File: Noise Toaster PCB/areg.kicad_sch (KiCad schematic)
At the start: 18 parts, among them Q1 2N3906, Q9 2N5457, U2 LM324

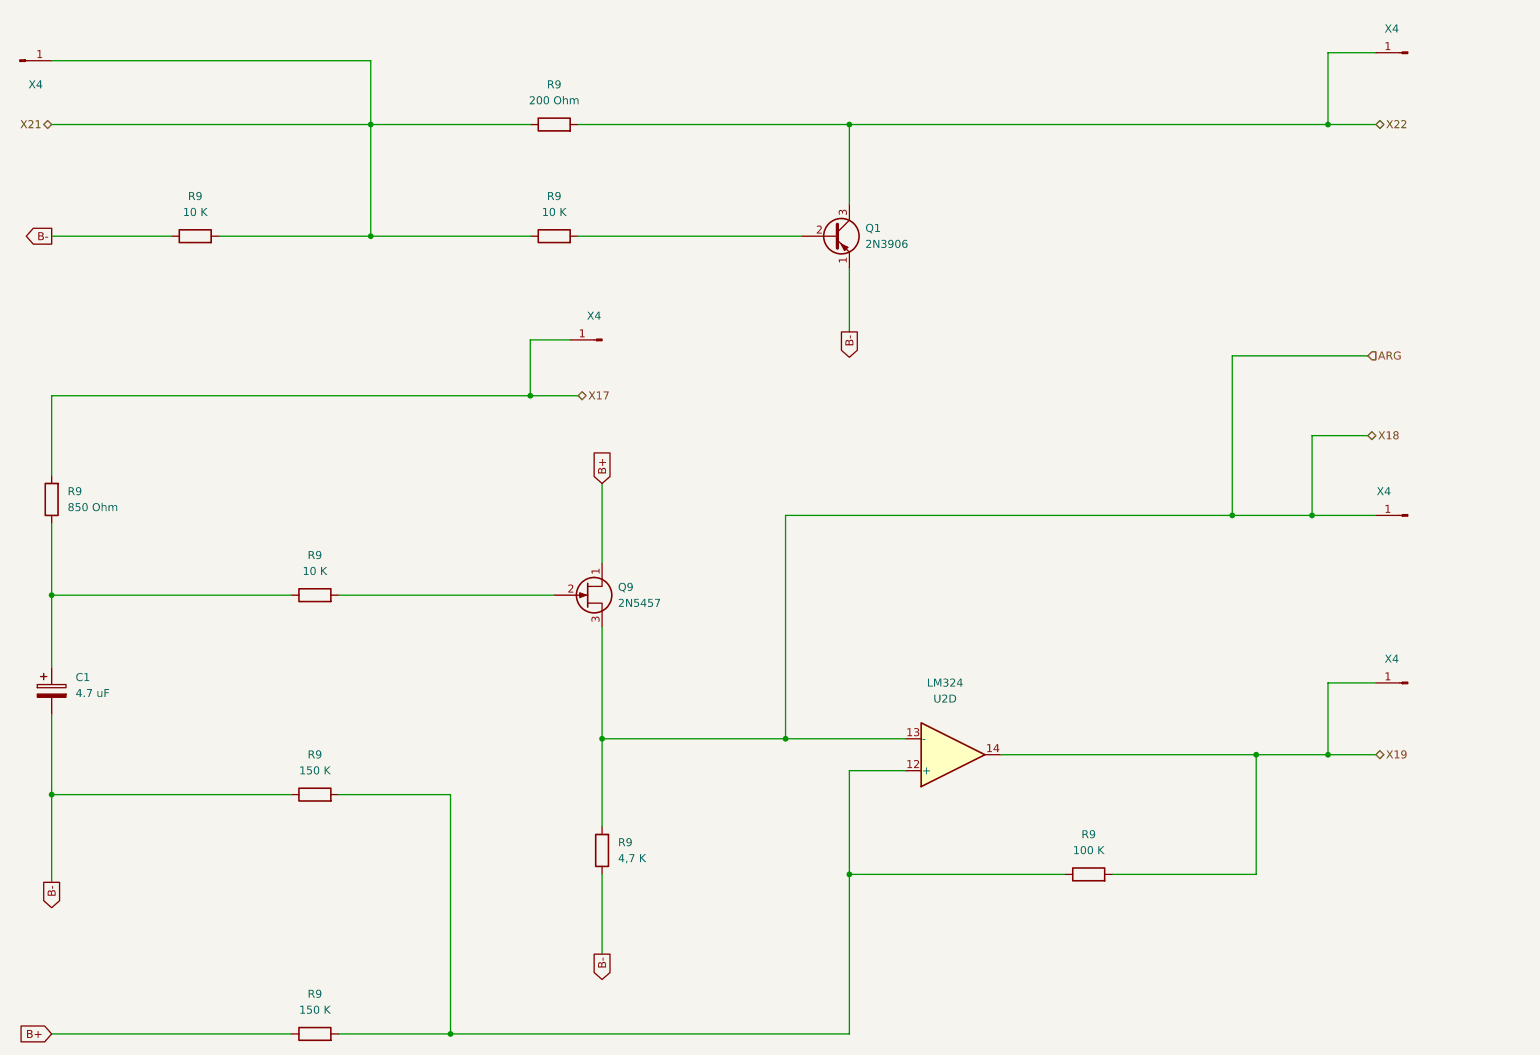
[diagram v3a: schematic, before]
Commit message: wireing and components have been checked
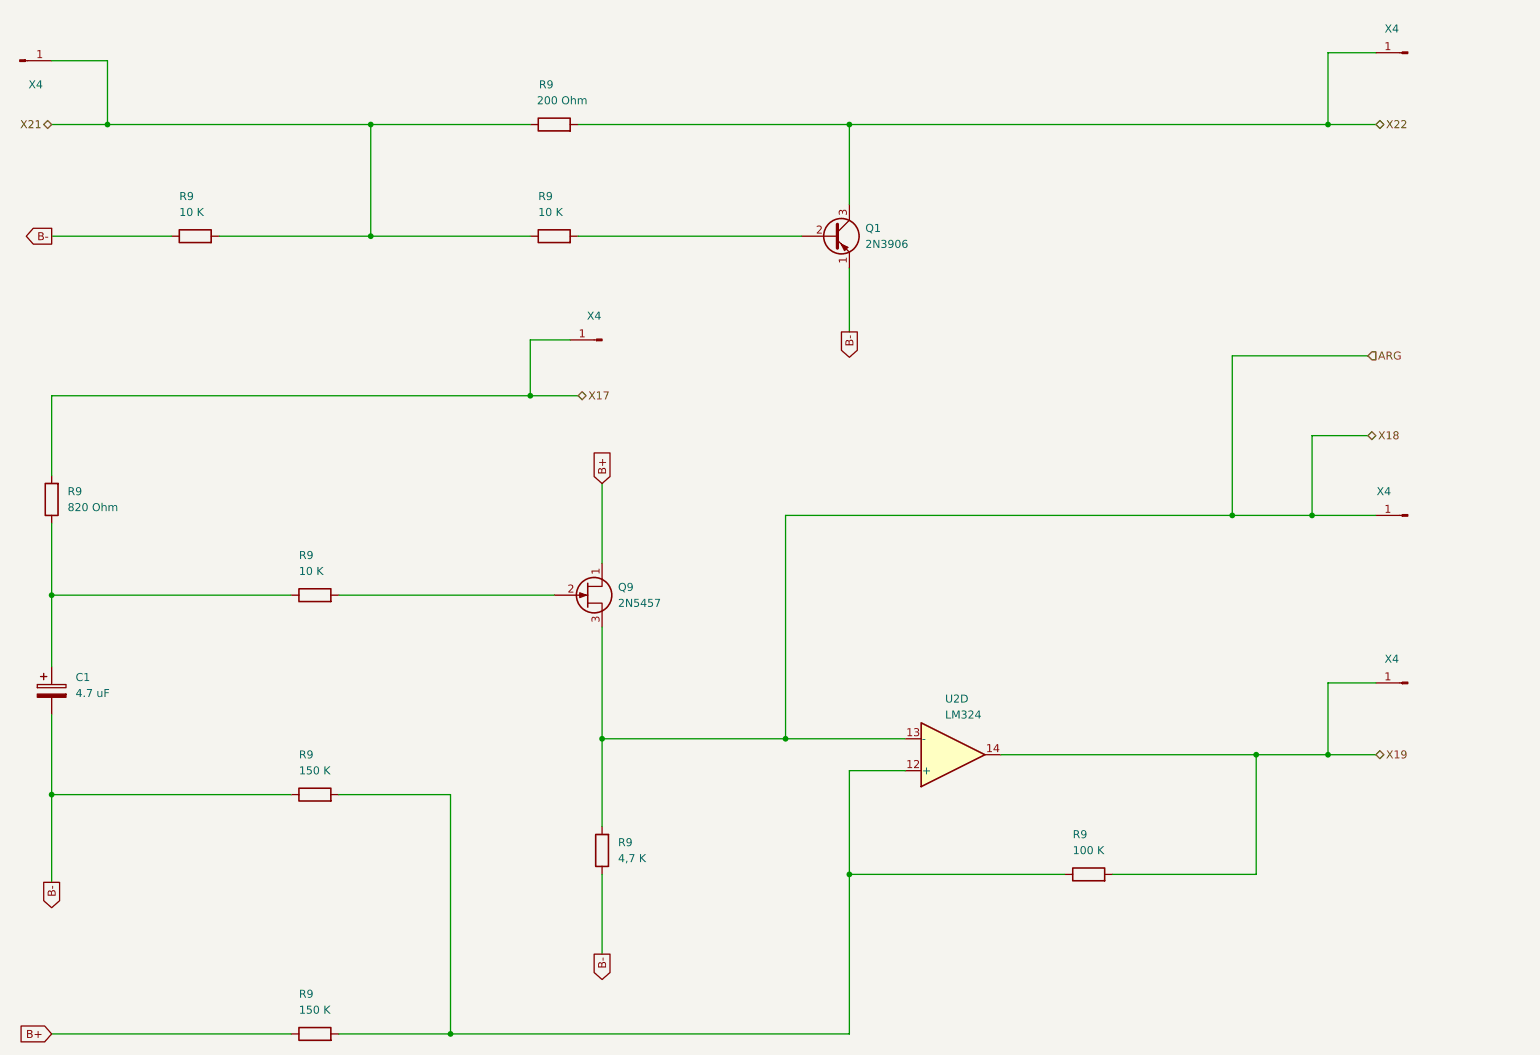
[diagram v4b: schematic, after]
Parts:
- R9: value 850 Ohm -> 820 Ohm
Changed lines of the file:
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@@
   (junction (at 241.3 33.02) (diameter 0) (color 0 0 0 0)
   )
+  (junction (at 46.99 33.02) (diameter 0) (color 0 0 0 0)
+  )
   (junction (at 114.3 76.2) (diameter 0) (color 0 0 0 0)
   )
@@
     (stroke (width 0) (type default))
   )
-  (wire (pts (xy 88.9 22.86) (xy 88.9 33.02))
+  (wire (pts (xy 46.99 22.86) (xy 46.99 33.02))
     (stroke (width 0) (type default))
   )
@@
     (stroke (width 0) (type default))
   )
-  (wire (pts (xy 38.1 33.02) (xy 88.9 33.02))
+  (wire (pts (xy 38.1 33.02) (xy 46.99 33.02))
     (stroke (width 0) (type default))
   )
@@
     (stroke (width 0) (type default))
   )
-  (wire (pts (xy 38.1 22.86) (xy 88.9 22.86))
+  (wire (pts (xy 38.1 22.86) (xy 46.99 22.86))
     (stroke (width 0) (type default))
   )
@@
   )
   (wire (pts (xy 114.3 76.2) (xy 121.92 76.2))
+    (stroke (width 0) (type default))
+  )
+  (wire (pts (xy 46.99 33.02) (xy 88.9 33.02))
     (stroke (width 0) (type default))
   )
@@
     (in_bom yes) (on_board yes) (dnp no)
     (property "Reference" "U2" (at 180.34 124.46 0)
-      (effects (font (size 1.27 1.27)))
-    )
-    (property "Value" "LM324" (at 180.34 121.92 0)
-      (effects (font (size 1.27 1.27)))
+      (effects (font (size 1.27 1.27)) (justify left))
+    )
+    (property "Value" "LM324" (at 180.34 127 0)
+      (effects (font (size 1.27 1.27)) (justify left))
     )
     (property "Footprint" "" (at 180.34 135.89 0)
@@
   )
   (symbol (lib_id "Device:R") (at 60.96 50.8 90) (unit 1)
-    (in_bom yes) (on_board yes) (dnp no) (fields_autoplaced)
-    (property "Reference" "R9" (at 60.96 44.45 90)
-      (effects (font (size 1.27 1.27)))
-    )
-    (property "Value" "10 K" (at 60.96 46.99 90)
-      (effects (font (size 1.27 1.27)))
+    (in_bom yes) (on_board yes) (dnp no)
+    (property "Reference" "R9" (at 58.42 44.45 90)
+      (effects (font (size 1.27 1.27)) (justify right))
+    )
+    (property "Value" "10 K" (at 58.42 46.99 90)
+      (effects (font (size 1.27 1.27)) (justify right))
     )
     (property "Footprint" "" (at 60.96 52.578 90)
@@
       (effects (font (size 1.27 1.27)) (justify right))
     )
-    (property "Value" "850 Ohm" (at 40.64 93.98 0)
+    (property "Value" "820 Ohm" (at 40.64 93.98 0)
       (effects (font (size 1.27 1.27)) (justify right))
     )
@@
   (symbol (lib_id "Device:R") (at 80.01 139.7 90) (unit 1)
     (in_bom yes) (on_board yes) (dnp no)
-    (property "Reference" "R9" (at 80.01 133.35 90)
-      (effects (font (size 1.27 1.27)))
-    )
-    (property "Value" "150 K" (at 80.01 135.89 90)
-      (effects (font (size 1.27 1.27)))
+    (property "Reference" "R9" (at 77.47 133.35 90)
+      (effects (font (size 1.27 1.27)) (justify right))
+    )
+    (property "Value" "150 K" (at 77.47 135.89 90)
+      (effects (font (size 1.27 1.27)) (justify right))
     )
     (property "Footprint" "" (at 80.01 141.478 90)
@@
   )
   (symbol (lib_id "Device:R") (at 80.01 107.95 90) (unit 1)
-    (in_bom yes) (on_board yes) (dnp no) (fields_autoplaced)
-    (property "Reference" "R9" (at 80.01 101.6 90)
-      (effects (font (size 1.27 1.27)))
-    )
-    (property "Value" "10 K" (at 80.01 104.14 90)
-      (effects (font (size 1.27 1.27)))
+    (in_bom yes) (on_board yes) (dnp no)
+    (property "Reference" "R9" (at 77.47 101.6 90)
+      (effects (font (size 1.27 1.27)) (justify right))
+    )
+    (property "Value" "10 K" (at 77.47 104.14 90)
+      (effects (font (size 1.27 1.27)) (justify right))
     )
     (property "Footprint" "" (at 80.01 109.728 90)
@@
   )
   (symbol (lib_id "Device:R") (at 118.11 50.8 90) (unit 1)
-    (in_bom yes) (on_board yes) (dnp no) (fields_autoplaced)
-    (property "Reference" "R9" (at 118.11 44.45 90)
-      (effects (font (size 1.27 1.27)))
-    )
-    (property "Value" "10 K" (at 118.11 46.99 90)
-      (effects (font (size 1.27 1.27)))
+    (in_bom yes) (on_board yes) (dnp no)
+    (property "Reference" "R9" (at 115.57 44.45 90)
+      (effects (font (size 1.27 1.27)) (justify right))
+    )
+    (property "Value" "10 K" (at 115.57 46.99 90)
+      (effects (font (size 1.27 1.27)) (justify right))
     )
     (property "Footprint" "" (at 118.11 52.578 90)
@@
   )
   (symbol (lib_id "Device:R") (at 203.2 152.4 90) (unit 1)
-    (in_bom yes) (on_board yes) (dnp no) (fields_autoplaced)
-    (property "Reference" "R9" (at 203.2 146.05 90)
-      (effects (font (size 1.27 1.27)))
-    )
-    (property "Value" "100 K" (at 203.2 148.59 90)
-      (effects (font (size 1.27 1.27)))
+    (in_bom yes) (on_board yes) (dnp no)
+    (property "Reference" "R9" (at 200.66 146.05 90)
+      (effects (font (size 1.27 1.27)) (justify right))
+    )
+    (property "Value" "100 K" (at 200.66 148.59 90)
+      (effects (font (size 1.27 1.27)) (justify right))
     )
     (property "Footprint" "" (at 203.2 154.178 90)
@@
   )
   (symbol (lib_id "Device:R") (at 118.11 33.02 90) (unit 1)
-    (in_bom yes) (on_board yes) (dnp no) (fields_autoplaced)
-    (property "Reference" "R9" (at 118.11 26.67 90)
-      (effects (font (size 1.27 1.27)))
-    )
-    (property "Value" "200 Ohm" (at 118.11 29.21 90)
+    (in_bom yes) (on_board yes) (dnp no)
+    (property "Reference" "R9" (at 116.84 26.67 90)
+      (effects (font (size 1.27 1.27)))
+    )
+    (property "Value" "200 Ohm" (at 119.38 29.21 90)
       (effects (font (size 1.27 1.27)))
     )
@@
   )
   (symbol (lib_id "Device:R") (at 80.01 177.8 90) (unit 1)
-    (in_bom yes) (on_board yes) (dnp no) (fields_autoplaced)
-    (property "Reference" "R9" (at 80.01 171.45 90)
-      (effects (font (size 1.27 1.27)))
-    )
-    (property "Value" "150 K" (at 80.01 173.99 90)
-      (effects (font (size 1.27 1.27)))
+    (in_bom yes) (on_board yes) (dnp no)
+    (property "Reference" "R9" (at 77.47 171.45 90)
+      (effects (font (size 1.27 1.27)) (justify right))
+    )
+    (property "Value" "150 K" (at 77.47 173.99 90)
+      (effects (font (size 1.27 1.27)) (justify right))
     )
     (property "Footprint" "" (at 80.01 179.578 90)

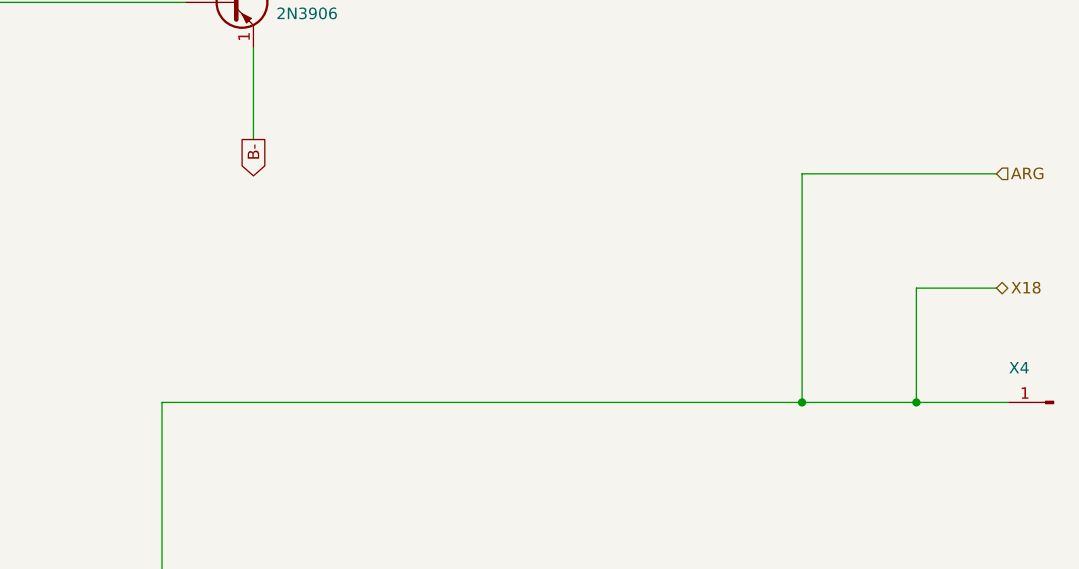
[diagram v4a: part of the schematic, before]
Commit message: applied footprints
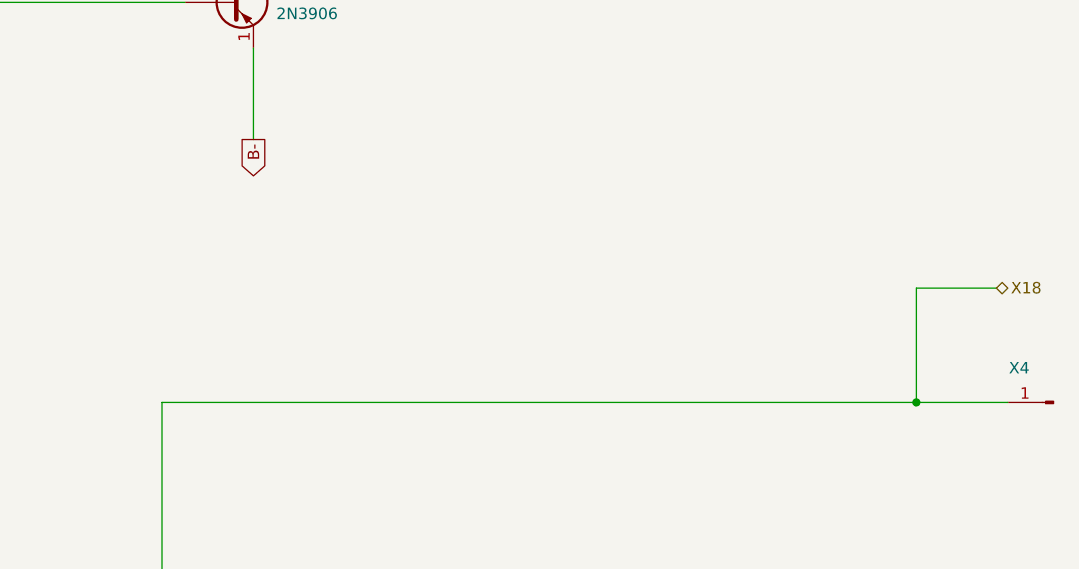
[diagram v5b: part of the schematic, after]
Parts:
- C1: footprint (none) -> Capacitor_THT:CP_Radial_D4.0mm_P1.50mm
- Q9: footprint (none) -> Package_TO_SOT_THT:TO-92_Inline
- R9: footprint (none) -> Resistor_THT:R_Axial_DIN0207_L6.3mm_D2.5mm_P10.16mm_Horizontal
- U2: footprint (none) -> Package_DIP:DIP-14_W7.62mm_Socket
- X4: footprint (none) -> Connector_PinHeader_1.00mm:PinHeader_1x01_P1.00mm_Vertical
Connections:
- net ARG renamed X18
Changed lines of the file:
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@@
   (junction (at 238.76 95.25) (diameter 0) (color 0 0 0 0)
   )
-  (junction (at 226.06 95.25) (diameter 0) (color 0 0 0 0)
-  )
   (junction (at 241.3 133.35) (diameter 0) (color 0 0 0 0)
   )
@@
     (stroke (width 0) (type default))
   )
-  (wire (pts (xy 226.06 69.85) (xy 226.06 95.25))
-    (stroke (width 0) (type default))
-  )
   (wire (pts (xy 248.92 95.25) (xy 238.76 95.25))
     (stroke (width 0) (type default))
@@
     (stroke (width 0) (type default))
   )
-  (wire (pts (xy 226.06 95.25) (xy 238.76 95.25))
+  (wire (pts (xy 154.94 95.25) (xy 238.76 95.25))
     (stroke (width 0) (type default))
   )
@@
     (stroke (width 0) (type default))
   )
-  (wire (pts (xy 154.94 95.25) (xy 226.06 95.25))
-    (stroke (width 0) (type default))
-  )
   (wire (pts (xy 125.73 130.81) (xy 154.94 130.81))
     (stroke (width 0) (type default))
@@
   )
   (wire (pts (xy 165.1 152.4) (xy 165.1 177.8))
-    (stroke (width 0) (type default))
-  )
-  (wire (pts (xy 247.65 69.85) (xy 226.06 69.85))
     (stroke (width 0) (type default))
   )
@@
     )
   )
-  (hierarchical_label "ARG" (shape input) (at 247.65 69.85 0) (fields_autoplaced)
-    (effects (font (size 1.27 1.27)) (justify left))
-  )
   (hierarchical_label "X22" (shape bidirectional) (at 248.92 33.02 0) (fields_autoplaced)
     (effects (font (size 1.27 1.27)) (justify left))
@@
       (effects (font (size 1.27 1.27)))
     )
-    (property "Footprint" "" (at 33.02 22.86 0)
+    (property "Footprint" "Connector_PinHeader_1.00mm:PinHeader_1x01_P1.00mm_Vertical" (at 33.02 22.86 0)
       (effects (font (size 1.27 1.27)) hide)
     )
@@
       (effects (font (size 1.27 1.27)) (justify left))
     )
-    (property "Footprint" "" (at 180.34 135.89 0)
+    (property "Footprint" "Package_DIP:DIP-14_W7.62mm_Socket" (at 180.34 135.89 0)
       (effects (font (size 1.27 1.27)) hide)
     )
@@
       (effects (font (size 1.27 1.27)) (justify left))
     )
-    (property "Footprint" "" (at 39.0652 127 0)
+    (property "Footprint" "Capacitor_THT:CP_Radial_D4.0mm_P1.50mm" (at 39.0652 127 0)
       (effects (font (size 1.27 1.27)) hide)
     )
@@
       (effects (font (size 1.27 1.27)) (justify left))
     )
-    (property "Footprint" "" (at 128.27 105.41 0)
+    (property "Footprint" "Package_TO_SOT_THT:TO-92_Inline" (at 128.27 105.41 0)
       (effects (font (size 1.27 1.27)) hide)
     )
@@
       (effects (font (size 1.27 1.27)))
     )
-    (property "Footprint" "" (at 254 21.59 0)
+    (property "Footprint" "Connector_PinHeader_1.00mm:PinHeader_1x01_P1.00mm_Vertical" (at 254 21.59 0)
       (effects (font (size 1.27 1.27)) hide)
     )
@@
       (effects (font (size 1.27 1.27)) (justify right))
     )
-    (property "Footprint" "" (at 60.96 52.578 90)
+    (property "Footprint" "Resistor_THT:R_Axial_DIN0207_L6.3mm_D2.5mm_P10.16mm_Horizontal" (at 60.96 52.578 90)
       (effects (font (size 1.27 1.27)) hide)
     )
@@
       (effects (font (size 1.27 1.27)) (justify right))
     )
-    (property "Footprint" "" (at 39.878 92.71 90)
+    (property "Footprint" "Resistor_THT:R_Axial_DIN0207_L6.3mm_D2.5mm_P10.16mm_Horizontal" (at 39.878 92.71 90)
       (effects (font (size 1.27 1.27)) hide)
     )
@@
       (effects (font (size 1.27 1.27)))
     )
-    (property "Footprint" "" (at 254 121.92 0)
+    (property "Footprint" "Connector_PinHeader_1.00mm:PinHeader_1x01_P1.00mm_Vertical" (at 254 121.92 0)
       (effects (font (size 1.27 1.27)) hide)
     )
@@
       (effects (font (size 1.27 1.27)) (justify right))
     )
-    (property "Footprint" "" (at 80.01 141.478 90)
+    (property "Footprint" "Resistor_THT:R_Axial_DIN0207_L6.3mm_D2.5mm_P10.16mm_Horizontal" (at 80.01 141.478 90)
       (effects (font (size 1.27 1.27)) hide)
     )
@@
       (effects (font (size 1.27 1.27)) (justify right))
     )
-    (property "Footprint" "" (at 127.508 148.59 90)
+    (property "Footprint" "Resistor_THT:R_Axial_DIN0207_L6.3mm_D2.5mm_P10.16mm_Horizontal" (at 127.508 148.59 90)
       (effects (font (size 1.27 1.27)) hide)
     )
@@
       (effects (font (size 1.27 1.27)))
     )
-    (property "Footprint" "" (at 254 95.25 0)
+    (property "Footprint" "Connector_PinHeader_1.00mm:PinHeader_1x01_P1.00mm_Vertical" (at 254 95.25 0)
       (effects (font (size 1.27 1.27)) hide)
     )
@@
       (effects (font (size 1.27 1.27)) (justify right))
     )
-    (property "Footprint" "" (at 80.01 109.728 90)
+    (property "Footprint" "Resistor_THT:R_Axial_DIN0207_L6.3mm_D2.5mm_P10.16mm_Horizontal" (at 80.01 109.728 90)
       (effects (font (size 1.27 1.27)) hide)
     )
@@
       (effects (font (size 1.27 1.27)))
     )
-    (property "Footprint" "" (at 125.73 67.31 0)
+    (property "Footprint" "Connector_PinHeader_1.00mm:PinHeader_1x01_P1.00mm_Vertical" (at 125.73 67.31 0)
       (effects (font (size 1.27 1.27)) hide)
     )
@@
       (effects (font (size 1.27 1.27)) (justify right))
     )
-    (property "Footprint" "" (at 118.11 52.578 90)
+    (property "Footprint" "Resistor_THT:R_Axial_DIN0207_L6.3mm_D2.5mm_P10.16mm_Horizontal" (at 118.11 52.578 90)
       (effects (font (size 1.27 1.27)) hide)
     )
@@
       (effects (font (size 1.27 1.27)) (justify right))
     )
-    (property "Footprint" "" (at 203.2 154.178 90)
+    (property "Footprint" "Resistor_THT:R_Axial_DIN0207_L6.3mm_D2.5mm_P10.16mm_Horizontal" (at 203.2 154.178 90)
       (effects (font (size 1.27 1.27)) hide)
     )
@@
       (effects (font (size 1.27 1.27)))
     )
-    (property "Footprint" "" (at 118.11 34.798 90)
+    (property "Footprint" "Resistor_THT:R_Axial_DIN0207_L6.3mm_D2.5mm_P10.16mm_Horizontal" (at 118.11 34.798 90)
       (effects (font (size 1.27 1.27)) hide)
     )
@@
       (effects (font (size 1.27 1.27)) (justify right))
     )
-    (property "Footprint" "" (at 80.01 179.578 90)
-      (effects (font (size 1.27 1.27)) hide)
-    )
+    (property "Footprint" "Resistor_THT:R_Axial_DIN0207_L6.3mm_D2.5mm_P10.16mm_Horizontal" (at 80.01 179.578 90)
+      (effects (font (size 1.27 1.27)) hide)
+    )

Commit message: placed pards of the pcb properly
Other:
- company: http://musicfromouterspace.com/analogsynth_new/NOISETOASTER/NOISETOASTER.php -> Music From Outer Space LLC
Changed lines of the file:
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@@
     (title "Attack Release Envelope Generator")
     (rev "0.5")
-    (company "http://musicfromouterspace.com/analogsynth_new/NOISETOASTER/NOISETOASTER.php")
+    (company "Music From Outer Space LLC")
     (comment 1 "Licence: CC-BY-NC-SA")
     (comment 2 "Original Design by Ray Wilson")
-    (comment 3 "Music From Outer Space LLC")
+    (comment 3 "http://musicfromouterspace.com/analogsynth_new/NOISETOASTER/NOISETOASTER.php")
   )
   (junction (at 88.9 50.8) (diameter 0) (color 0 0 0 0)
